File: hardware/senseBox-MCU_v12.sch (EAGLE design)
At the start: 140 parts, among them IC1 VREG-AP2111H-3V3, IC2 ATSAMD21G18A-MU, IC3 MAX8XX-809R, IC4 MAX8XX-809R, IC5 74LVC244PW, IC6 BMX055, IC7 ATECC608A-MAHDA, J1 USB-MICROB-2, J10 JST4-B4B-PH-SM4-TB, J11 JST4-B4B-PH-SM4-TB, J12 JST4-B4B-PH-SM4-TB, J13 JST4-B4B-PH-SM4-TB, J14 JUMPER3-0402, J15 JUMPER3-0402, J2 JST2-B2B-PH-SM4-TB, J3 SWD-2X5-SMD, J4 JST4-B4B-PH-SM4-TB, J5 JST4-B4B-PH-SM4-TB, J6 JST4-B4B-PH-SM4-TB, J7 JST4-B4B-PH-SM4-TB, J8 JST4-B4B-PH-SM4-TB, J9 JST4-B4B-PH-SM4-TB, Q1 32.768KHz, SW1 PTS645SH50SMTR92-Grey, SW2 PTS645SK50SMTR92-Red, T1 BSS138PS, T2 P-Chn, T3 P-Chn, T4 P-Chn, T5 BSS138PS, T6 BSS138PS, T7 P-Chn, X1 PASSER-07, X2 PASSER-07, X3 PASSER-07, X4 PASSER-07

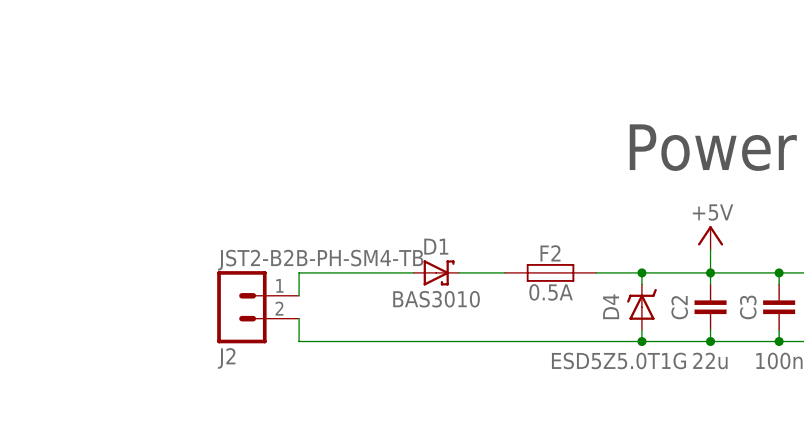
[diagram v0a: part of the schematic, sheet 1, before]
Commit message: merge watterott changes by overwriting changed files
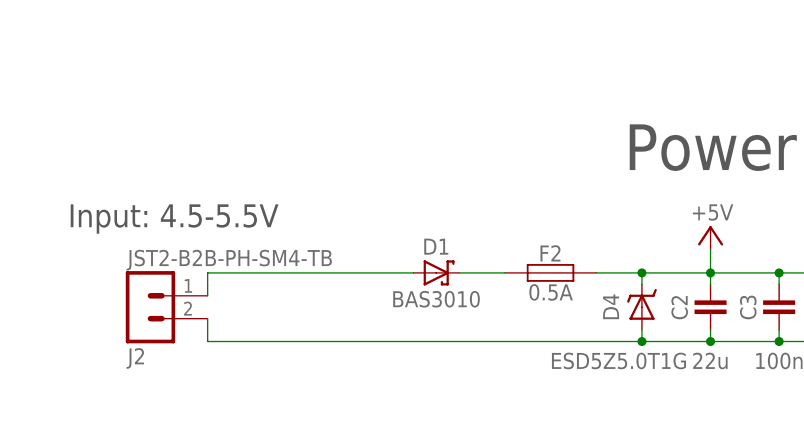
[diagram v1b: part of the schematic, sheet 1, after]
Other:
- note added: "Input: 4.5-5.5V"
- moved on the sheet: J2
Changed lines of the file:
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@@
 <setting verticaltext="up"/>
 </settings>
-<grid distance="0.1" unitdist="inch" unit="inch" style="lines" multiple="1" display="no" altdistance="0.01" altunitdist="inch" altunit="inch"/>
+<grid distance="0.05" unitdist="inch" unit="inch" style="lines" multiple="1" display="yes" altdistance="0.01" altunitdist="inch" altunit="inch"/>
 <layers>
 <layer number="1" name="Top" color="4" fill="1" visible="no" active="no"/>
@@
 <text x="170.18" y="165.1" size="5.08" layer="97" ratio="20" align="center">SAMD21</text>
 <text x="81.28" y="33.02" size="5.08" layer="97" ratio="20" align="center">Power</text>
+<text x="21.59" y="25.4" size="2.54" layer="97" ratio="20" align="center">Input: 4.5-5.5V</text>
 </plain>
 <instances>
@@
 <attribute name="VALUE" x="127" y="10.16" size="1.778" layer="96" align="top-center"/>
 </instance>
-<instance part="J2" gate="J" x="27.94" y="13.97" rot="MR180"/>
+<instance part="J2" gate="J" x="17.78" y="13.97" rot="MR180"/>
 <instance part="R4" gate="R" x="52.07" y="58.42"/>
 <instance part="GND5" gate="1" x="69.85" y="55.88" smashed="yes">
@@
 <pinref part="C2" gate="C" pin="1"/>
 <pinref part="C9" gate="C" pin="1"/>
-<wire x1="73.66" y1="11.43" x2="35.56" y2="11.43" width="0.1524" layer="91"/>
+<wire x1="73.66" y1="11.43" x2="25.4" y2="11.43" width="0.1524" layer="91"/>
 <pinref part="D4" gate="D" pin="A"/>
 <wire x1="73.66" y1="11.43" x2="73.66" y2="12.7" width="0.1524" layer="91"/>
@@
 <junction x="127" y="11.43"/>
 <pinref part="J2" gate="J" pin="2"/>
-<wire x1="35.56" y1="11.43" x2="35.56" y2="13.97" width="0.1524" layer="91"/>
+<wire x1="25.4" y1="11.43" x2="25.4" y2="13.97" width="0.1524" layer="91"/>
 </segment>
 <segment>
@@
 <pinref part="D1" gate="D" pin="A"/>
 <pinref part="J2" gate="J" pin="1"/>
-<wire x1="48.26" y1="19.05" x2="35.56" y2="19.05" width="0.1524" layer="91"/>
-<wire x1="35.56" y1="19.05" x2="35.56" y2="16.51" width="0.1524" layer="91"/>
-</segment>
-</net>
+<wire x1="48.26" y1="19.05" x2="25.4" y2="19.05" width="0.1524" layer="91"/>
+<wire x1="25.4" y1="19.05" x2="25.4" y2="16.51" width="0.1524" layer="91"/>
+</segment>
+</net>
